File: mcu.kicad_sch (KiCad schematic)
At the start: 33 parts

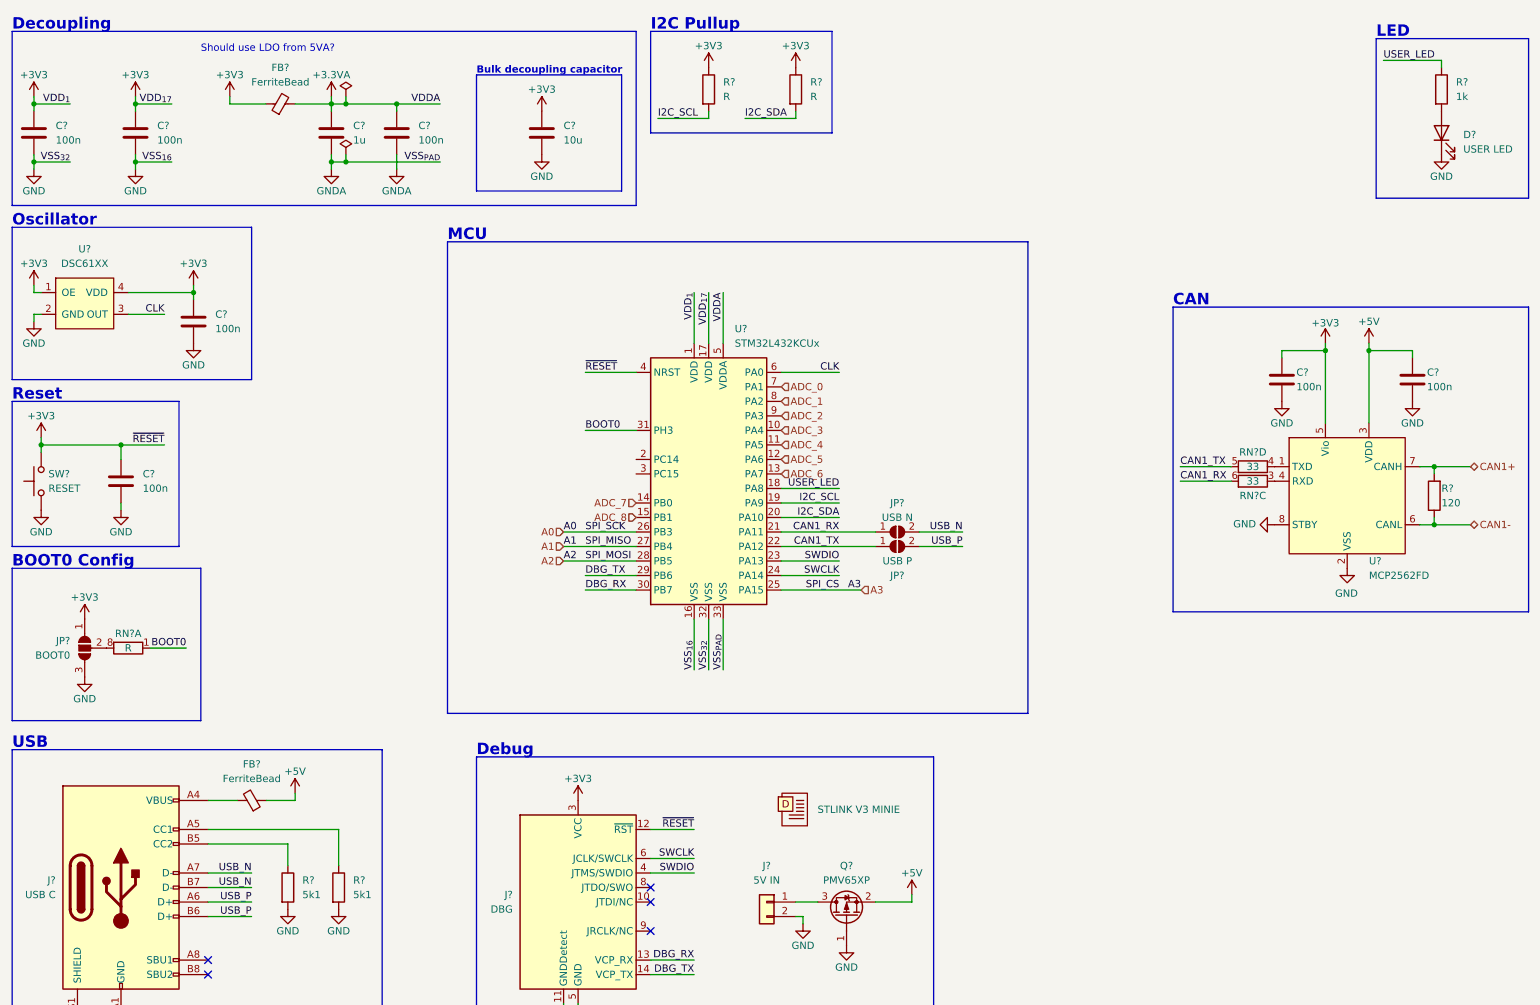
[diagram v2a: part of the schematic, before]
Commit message: sch: input stage sheets
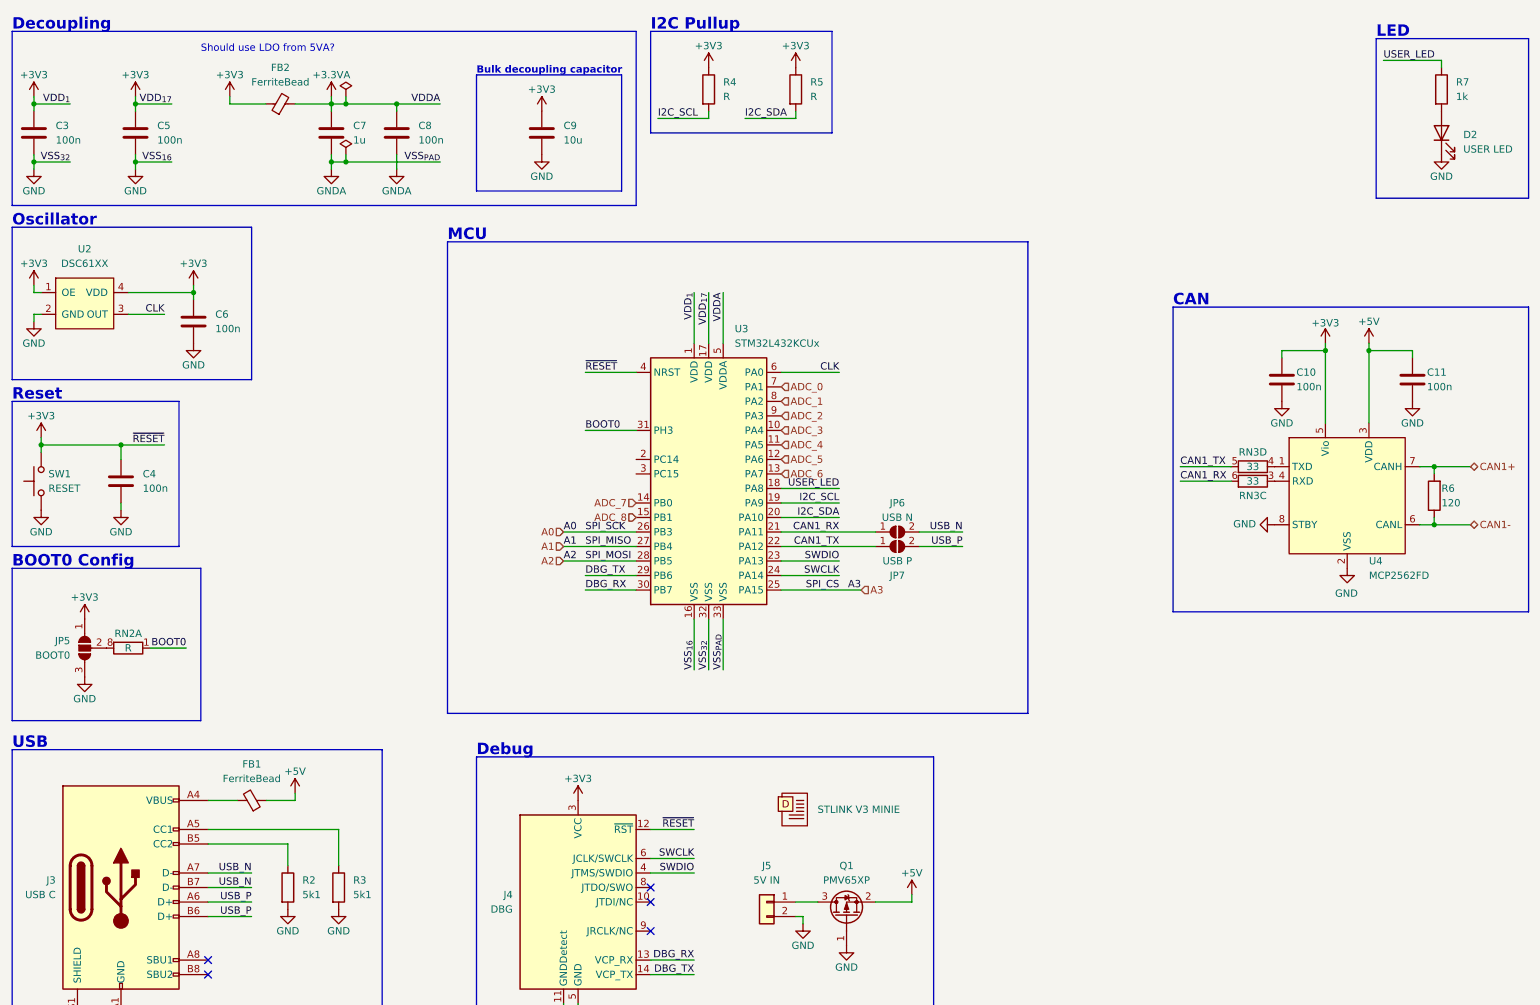
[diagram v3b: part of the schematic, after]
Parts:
- D1: renamed from D?; now left out of the parts list
- D2: renamed from D?; footprint (none) -> LED_SMD:LED_0603_1608Metric
- FB1, FB2: renamed from FB?; footprint (none) -> Inductor_SMD:L_0603_1608Metric
- J4: renamed from J?; footprint (none) -> Eagle_Connectors:SAMTEC_FTSH-107-01-L-DV-K-TR
- J5: renamed from J?; footprint (none) -> Connector_PinHeader_2.54mm:PinHeader_1x02_P2.54mm_Vertical
- JP5: renamed from JP?; footprint (none) -> Jumper:SolderJumper-3_P1.3mm_Open_RoundedPad1.0x1.5mm
- JP6, JP7: renamed from JP?; footprint (none) -> Jumper:SolderJumper-2_P1.3mm_Open_RoundedPad1.0x1.5mm
- RN2: renamed from RN?; footprint (none) -> Resistor_SMD:R_Array_Convex_4x0603
- SW1: renamed from SW?; footprint (none) -> Button_Switch_SMD:SW_SPST_FSMSM
- gave numbers to parts that had none: 21

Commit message: sch: add power delivery network and finalize schematic
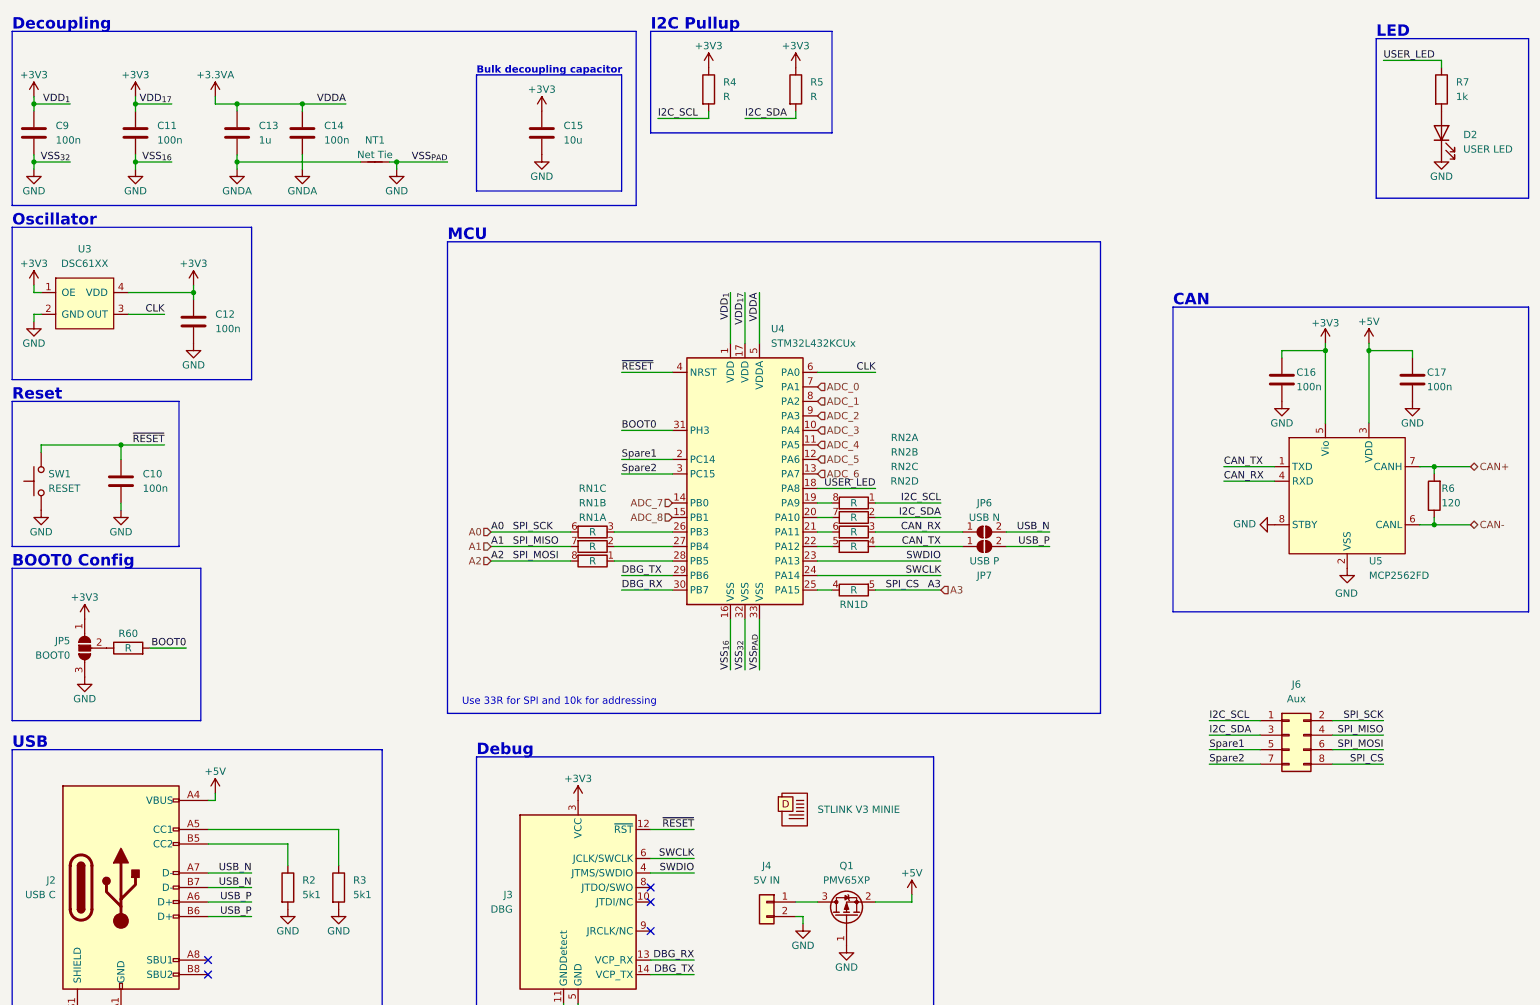
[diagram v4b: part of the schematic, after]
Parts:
- removed FB1, FB2: FerriteBead, Inductor_SMD:L_0603_1608Metric, symbol Device:FerriteBead_Small
- removed RN3: 33, Resistor_SMD:R_Array_Convex_4x0603, symbol Device:R_Pack04_Split
- added J6: Aux, Connector_PinHeader_2.54mm:PinHeader_2x04_P2.54mm_Vertical, symbol Connector_Generic:Conn_02x04_Odd_Even
- added NT1: Net Tie, NetTie:NetTie-2_SMD_Pad0.5mm, symbol Device:NetTie_2
- added R60: R, Resistor_SMD:R_0603_1608Metric, symbol Device:R
- added RN1: R, Resistor_SMD:R_Array_Convex_4x0603, symbol Device:R_Pack04_Split
- added unit 4 of RN2
- added unit 2 of RN2
- added unit 3 of RN2
- C13: renamed from C7; footprint Capacitor_SMD:C_0603_1608Metric -> Capacitor_SMD:C_0805_2012Metric
- J2: renamed from J3; footprint (none) -> Connector_USB:USB_C_Receptacle_HRO_TYPE-C-31-M-12
- U3: renamed from U2; footprint (none) -> Package_LGA:VLGA-4_2x2.5mm_P1.65mm
- U4: renamed from U3; Secondary Datasheet (none) -> docs/application-notes/an4555_stm32l4x-hw-design-guide.pdf
- renumbered C4 to C10, C5 to C11, C6 to C12, C8 to C14, C9 to C15, C10 to C16, C11 to C17, C3 to C9, J4 to J3, J5 to J4, U4 to U5
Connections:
- net +3V3: no longer C10.1, J3.12 (~{RST}), SW1.2, U4.4 (NRST)
- net +5V: now also J2.A4 (VBUS), J2.A9 (VBUS), J2.B4 (VBUS), J2.B9 (VBUS)
- net A0: now also J6.2 (Pin_2), RN1.6 (R3.2); no longer U4.26 (PB3)
- net A1: now also J6.4 (Pin_4), RN1.7 (R2.2); no longer U4.27 (PB4)
- net A2: now also J6.6 (Pin_6), RN1.8 (R1.2); no longer U4.28 (PB5)
- net A3: now also J6.8 (Pin_8), RN1.5 (R4.2); no longer U4.25 (PA15)
- net BOOT0: now also R60.2; no longer RN2.1 (R1.1)
- net GND: now also U4.33 (VSS), NT1.1
- net GNDA: now also NT1.2; no longer U4.33 (VSS)
- net I2C_SCL: now also RN2.1 (R1.1), J6.1 (Pin_1); no longer U4.19 (PA9)
- net I2C_SDA: now also J6.3 (Pin_3), RN2.2 (R2.1); no longer U4.20 (PA10)
- net at JP5.2 (C): now also R60.1; no longer RN2.8 (R1.2)
- net Spare1: now reaches U4.2 (PC14)
- net Spare1: now also J6.5 (Pin_5)
- net Spare2: now reaches U4.3 (PC15)
- net Spare2: now also J6.7 (Pin_7)
- net CAN_TX: now reaches U5.1 (TXD)
- net CAN_TX: now also JP7.1 (A), RN2.4 (R4.1)
- net CAN_RX: now reaches U5.4 (RXD)
- net CAN_RX: now also JP6.1 (A), RN2.3 (R3.1)
- net CAN1+ renamed CAN+
- net CAN1- renamed CAN-
- net CAN1_RX: no longer names the net of U4.21 (PA11)
- net CAN1_RX: now also RN2.6 (R3.2); no longer JP6.1 (A)
- net CAN1_TX: no longer names the net of U4.22 (PA12)
- net CAN1_TX: now also RN2.5 (R4.2); no longer JP7.1 (A)
- new net: RN1.4 (R4.1), U4.25 (PA15)
- new net: RN1.1 (R1.1), U4.28 (PB5)
- new net: RN1.2 (R2.1), U4.27 (PB4)
- new net: RN1.3 (R3.1), U4.26 (PB3)
- new net: RN2.8 (R1.2), U4.19 (PA9)
- new net: RN2.7 (R2.2), U4.20 (PA10)
- new net ~{RESET}: C10.1, J3.12 (~{RST}), SW1.2, U4.4 (NRST)
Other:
- note added: "Use 33R for SPI and 10k for addressing"
- note removed: "Should use LDO from 5VA?"
- company: (none) -> E-Agle TRT
- title: (none) -> An2CAN
- moved on the sheet: C13, C14, JP6, JP7, U4

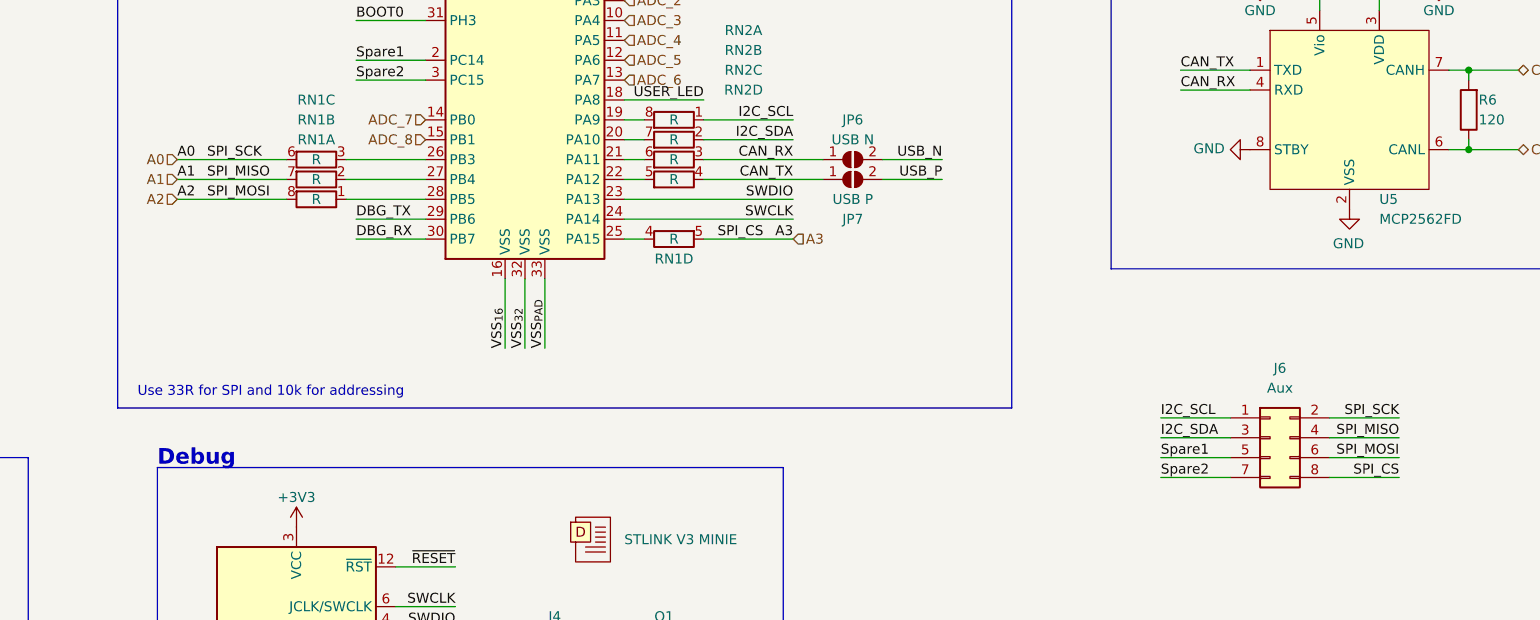
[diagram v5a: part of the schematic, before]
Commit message: pcb: continue routing of digital section
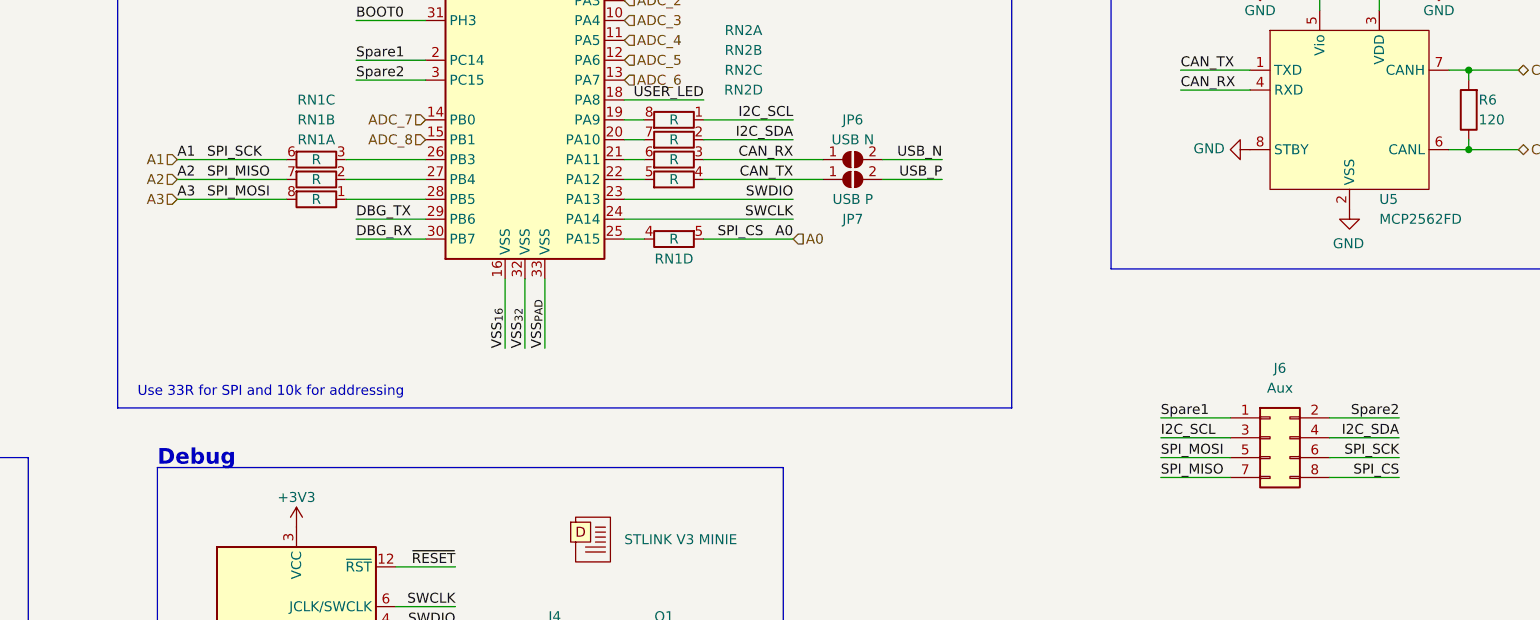
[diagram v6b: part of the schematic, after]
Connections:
- net A0: now also J6.8 (Pin_8), RN1.5 (R4.2); no longer J6.2 (Pin_2), RN1.6 (R3.2)
- net A1: now also J6.6 (Pin_6), RN1.6 (R3.2); no longer J6.4 (Pin_4), RN1.7 (R2.2)
- net A2: now also J6.7 (Pin_7), RN1.7 (R2.2); no longer J6.6 (Pin_6), RN1.8 (R1.2)
- net A3: now also J6.5 (Pin_5), RN1.8 (R1.2); no longer J6.8 (Pin_8), RN1.5 (R4.2)
- net I2C_SCL: now also J6.3 (Pin_3); no longer J6.1 (Pin_1)
- net I2C_SDA: now also J6.4 (Pin_4); no longer J6.3 (Pin_3)
- net Spare1: now also J6.1 (Pin_1); no longer J6.5 (Pin_5)
- net Spare2: now also J6.2 (Pin_2); no longer J6.7 (Pin_7)

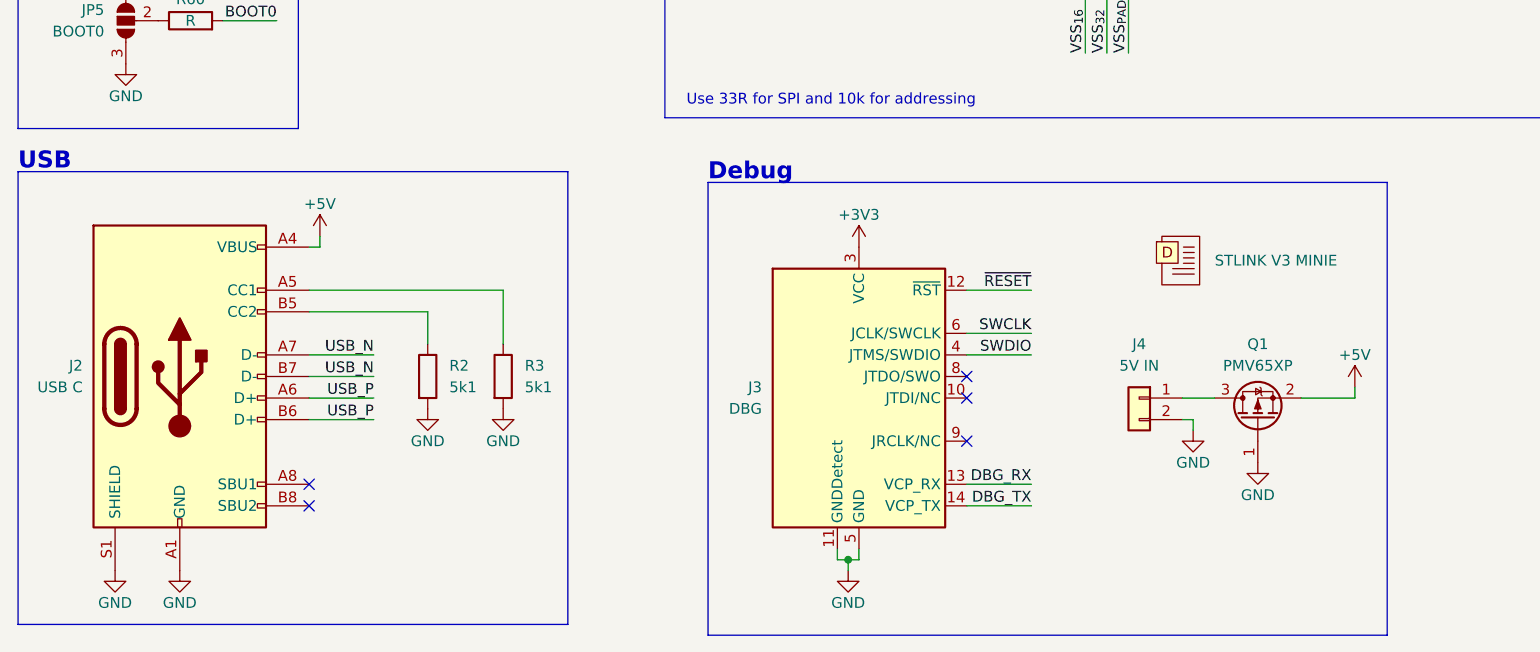
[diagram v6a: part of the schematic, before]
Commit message: pcb: complete routing, add silkscreen details, finalize board
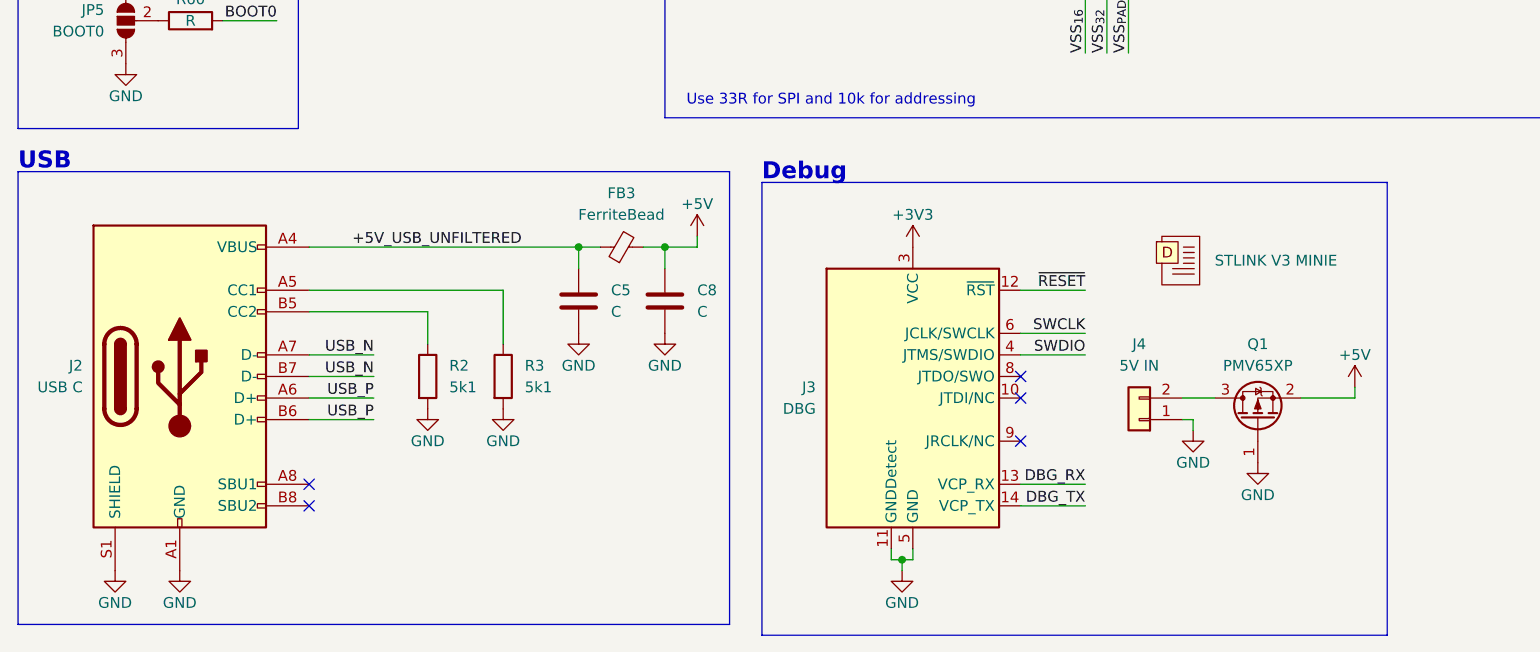
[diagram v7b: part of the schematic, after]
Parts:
- added C5, C8: C, Capacitor_SMD:C_0805_2012Metric, symbol Device:C
- added FB3: FerriteBead, Inductor_SMD:L_0603_1608Metric, symbol Device:FerriteBead_Small
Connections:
- net +5V: now also C8.1, FB3.2; no longer J2.A4 (VBUS), J2.A9 (VBUS), J2.B4 (VBUS), J2.B9 (VBUS)
- net GND: now also J4.1 (Pin_1), C5.2, C8.2; no longer J4.2 (Pin_2)
- net at Q1.3 (D): now also J4.2 (Pin_2); no longer J4.1 (Pin_1)
- new net +5V_USB_UNFILTERED: C5.1, FB3.1, J2.A4 (VBUS), J2.A9 (VBUS), J2.B4 (VBUS), J2.B9 (VBUS)
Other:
- moved on the sheet: J3, J4
